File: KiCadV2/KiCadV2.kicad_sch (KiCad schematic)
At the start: 48 parts, among them J1 USB_C_Receptacle_PowerOnly_6P, J3 Screw_Terminal_01x02, J4 Screw_Terminal_01x02, U1 MT3608, U14 74LV08AT14-13, U16 NC7SZ157P6X, U17 MX3502S, U18 MX3502S, U2 74HC595, U26 MX3502S, U3 NC7SZ157P6X, U38 74LV08AT14-13, U4 NC7SZ157P6X, U5 MX3502S, U6 NC7SZ157P6X, U7 DAC082S085CISDX/NOPB

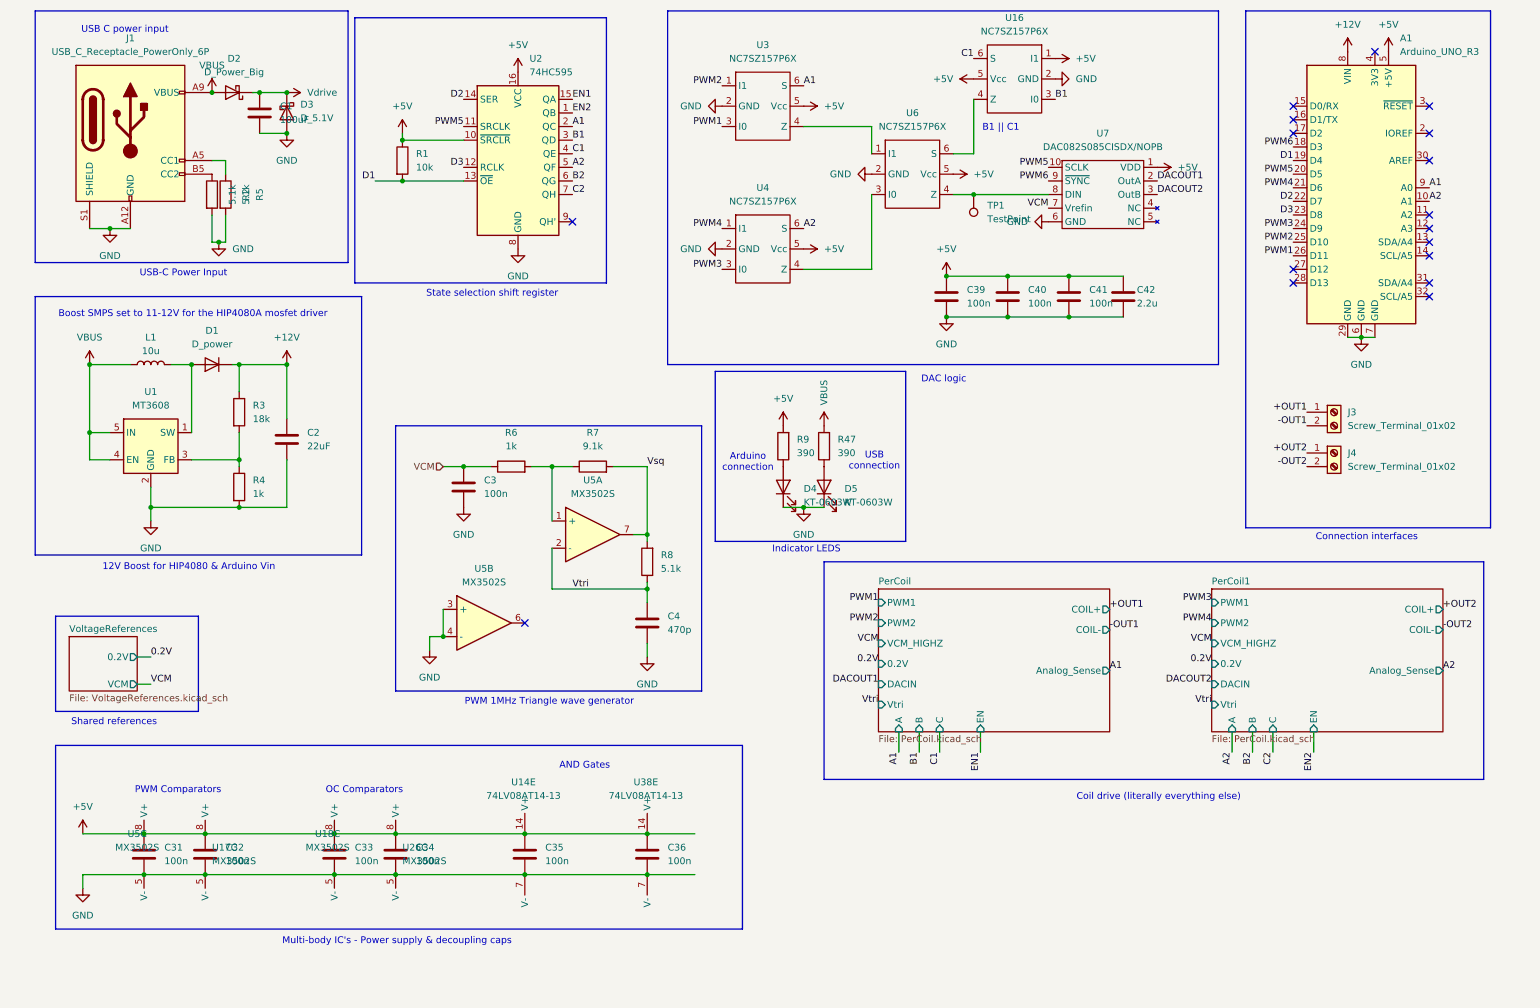
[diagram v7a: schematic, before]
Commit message: Made changes to schematic and just updated PCB from schematic. Haven't edited PCB yet.
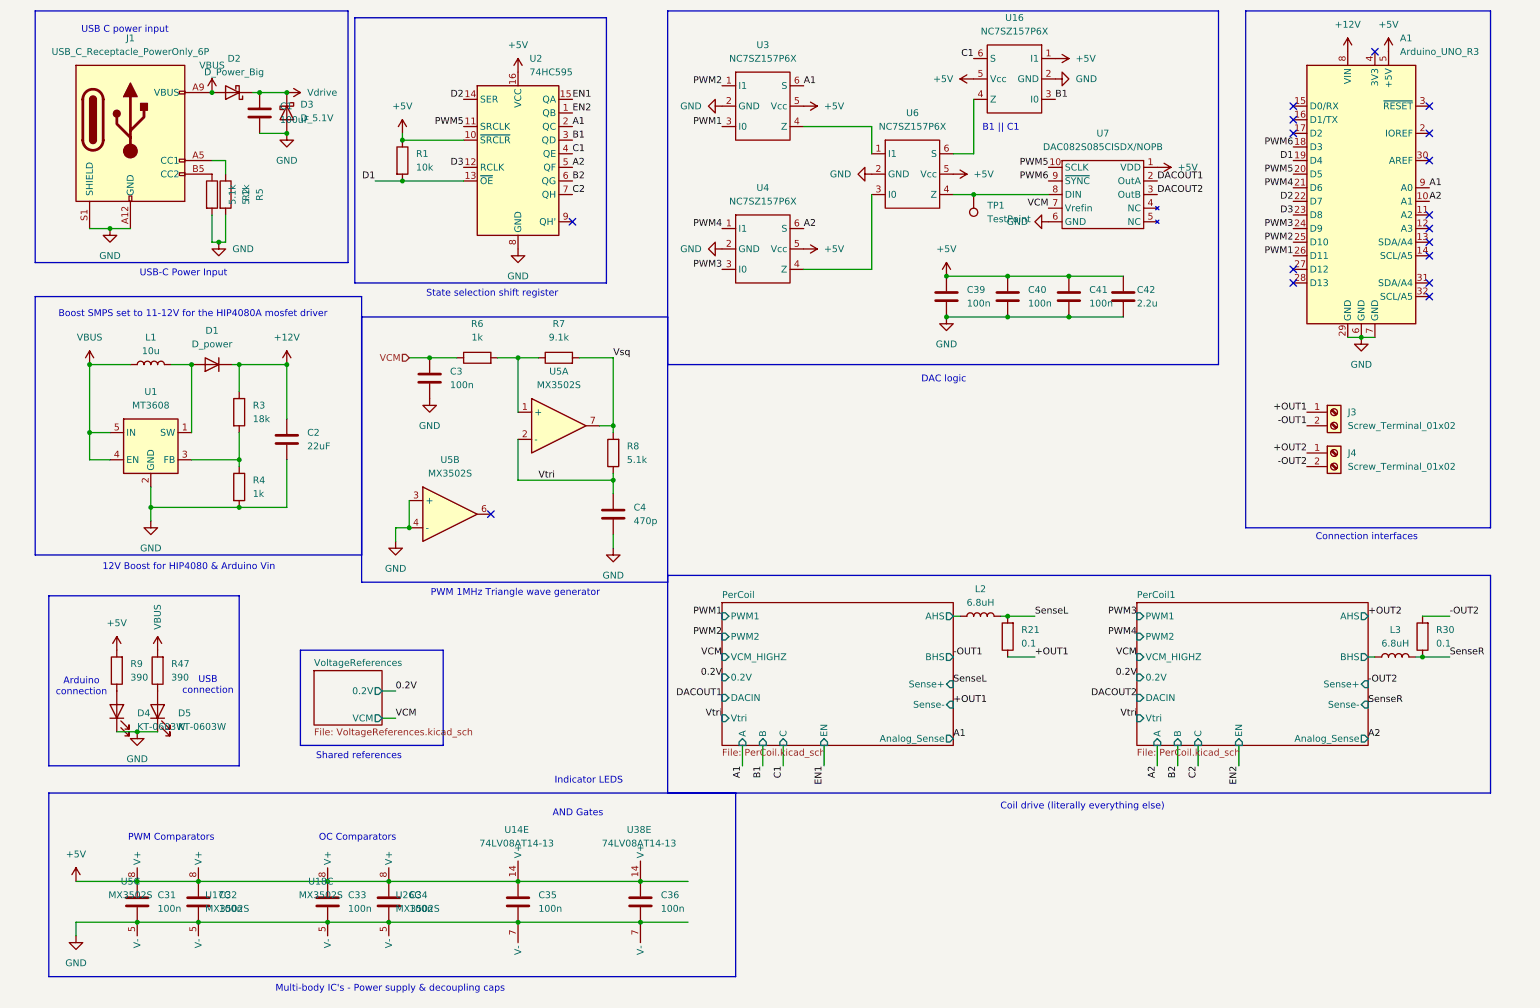
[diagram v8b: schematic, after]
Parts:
- added L2, L3: 6.8uH, Inductor_SMD:6.8uH C5127257, symbol Device:L
- added R21, R30: 0.1, Resistor_SMD:R_1206_3216Metric, symbol Device:R
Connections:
- net +OUT1: now also R21.1
- net -OUT2: now also R30.2
- new net PerCoil/AHS: L2.1
- new net PerCoil1/BHS: L3.1
- new net SenseL: L2.2, R21.2
- new net SenseR: L3.2, R30.1
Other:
- sheet PerCoil ports: added AHS, BHS, Sense+, Sense-; removed COIL+, COIL-
- sheet PerCoil1 ports: added AHS, BHS, Sense+, Sense-; removed COIL+, COIL-
- moved on the sheet: C3, C31, C32, C33, C34, C35, C36, C4, D4, D5, R47, R6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
